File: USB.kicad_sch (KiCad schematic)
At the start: 20 parts, among them J501 USB_A_Stacked, J502 USB_A_Stacked, U501 ASDMB-24.000MHz-C, U502 ASDMB-26.000MHz-C, U503 USB3343, U504 74LVC1G07, U505 USB2514B_Bi

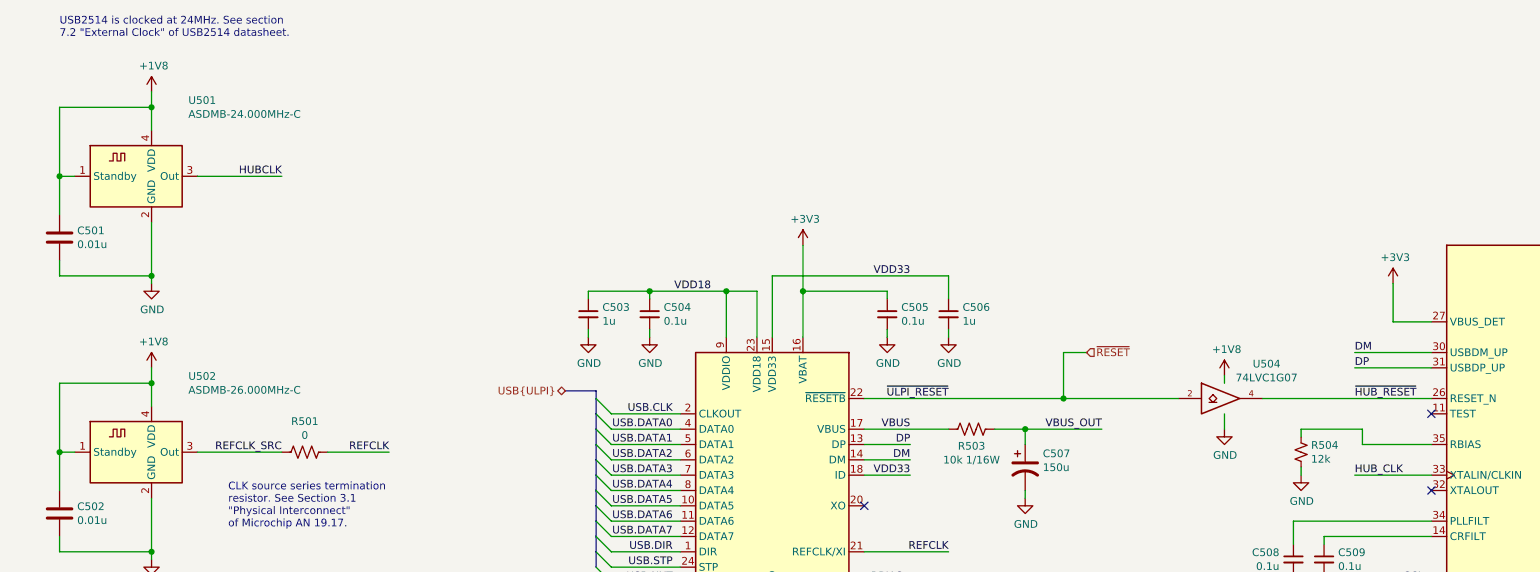
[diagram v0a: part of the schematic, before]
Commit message: Power USB REFCLK from PHY regulator, add pull up resistors to USB reset line
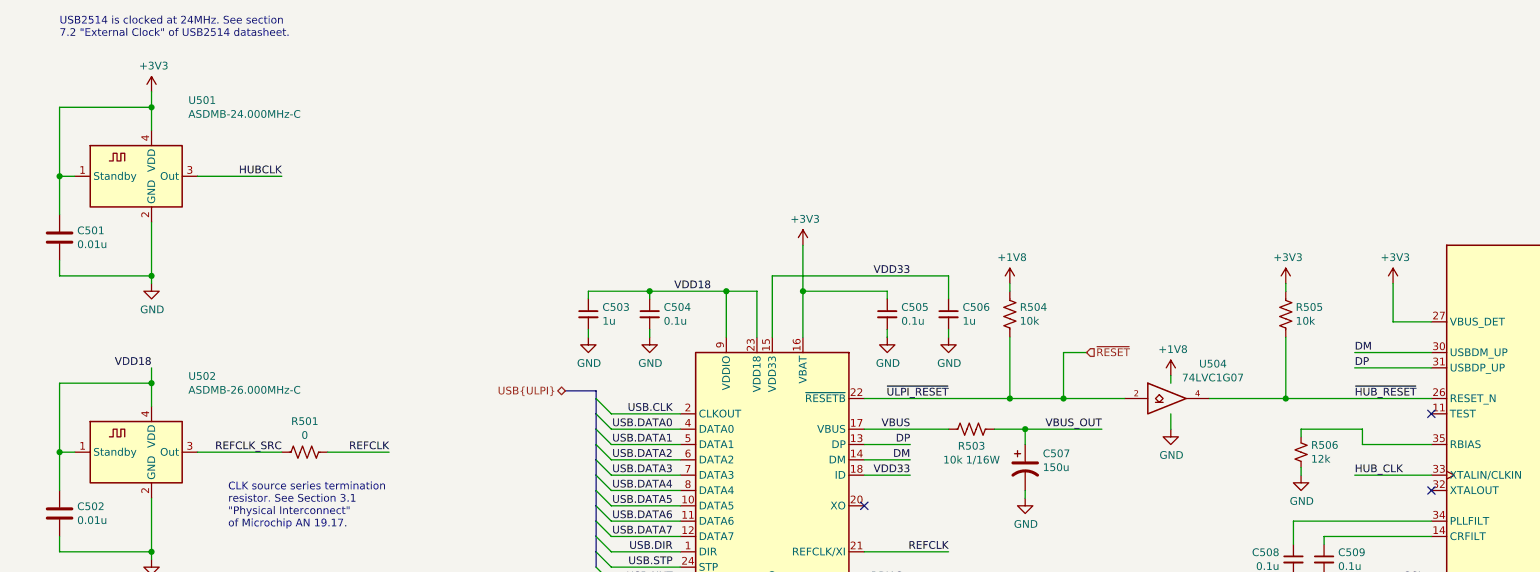
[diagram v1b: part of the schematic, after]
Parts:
- added R504, R505: 10k, Resistor_SMD:R_0402_1005Metric, symbol Device:R_US
- renumbered R504 to R506
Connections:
- net +1V8: now also R504.1; no longer C501.1, C502.1, U501.1 (Standby), U501.4 (VDD), U502.1 (Standby), U502.4 (VDD)
- net +3V3: now also C501.1, U501.1 (Standby), U501.4 (VDD), R505.1
- net VDD18: now also C502.1, U502.1 (Standby), U502.4 (VDD)
- net ~HUB_RESET: now also R505.2
- net ~RESET: now also R504.2
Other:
- moved on the sheet: U504
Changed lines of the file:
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@@
   (junction (at 156.21 99.06) (diameter 1.016) (color 0 0 0 0))
   (junction (at 168.91 99.06) (diameter 1.016) (color 0 0 0 0))
+  (junction (at 203.2 116.84) (diameter 1.016) (color 0 0 0 0))
   (junction (at 205.74 121.92) (diameter 1.016) (color 0 0 0 0))
   (junction (at 212.09 116.84) (diameter 1.016) (color 0 0 0 0))
+  (junction (at 248.92 116.84) (diameter 1.016) (color 0 0 0 0))
   (junction (at 252.73 148.59) (diameter 1.016) (color 0 0 0 0))
-  (no_connect (at 273.05 119.38))
   (no_connect (at 273.05 132.08))
   (no_connect (at 179.07 134.62))
+  (no_connect (at 273.05 119.38))
   (bus_entry (at 134.62 116.84) (size 2.54 2.54)
     (stroke (width 0.1524) (type solid) (color 0 0 0 0))
@@
     (stroke (width 0) (type solid) (color 0 0 0 0))
   )
-  (wire (pts (xy 179.07 116.84) (xy 212.09 116.84))
+  (wire (pts (xy 179.07 116.84) (xy 203.2 116.84))
     (stroke (width 0) (type solid) (color 0 0 0 0))
   )
@@
     (stroke (width 0) (type solid) (color 0 0 0 0))
   )
+  (wire (pts (xy 203.2 97.79) (xy 203.2 99.06))
+    (stroke (width 0) (type solid) (color 0 0 0 0))
+  )
+  (wire (pts (xy 203.2 106.68) (xy 203.2 116.84))
+    (stroke (width 0) (type solid) (color 0 0 0 0))
+  )
+  (wire (pts (xy 203.2 116.84) (xy 212.09 116.84))
+    (stroke (width 0) (type solid) (color 0 0 0 0))
+  )
   (wire (pts (xy 205.74 121.92) (xy 205.74 124.46))
     (stroke (width 0) (type solid) (color 0 0 0 0))
@@
     (stroke (width 0) (type solid) (color 0 0 0 0))
   )
-  (wire (pts (xy 212.09 116.84) (xy 231.14 116.84))
+  (wire (pts (xy 212.09 116.84) (xy 222.25 116.84))
     (stroke (width 0) (type solid) (color 0 0 0 0))
   )
@@
     (stroke (width 0) (type solid) (color 0 0 0 0))
   )
-  (wire (pts (xy 238.76 113.03) (xy 238.76 114.3))
-    (stroke (width 0) (type solid) (color 0 0 0 0))
-  )
-  (wire (pts (xy 238.76 119.38) (xy 238.76 121.92))
-    (stroke (width 0) (type solid) (color 0 0 0 0))
-  )
-  (wire (pts (xy 245.11 116.84) (xy 273.05 116.84))
+  (wire (pts (xy 229.87 113.03) (xy 229.87 114.3))
+    (stroke (width 0) (type solid) (color 0 0 0 0))
+  )
+  (wire (pts (xy 229.87 119.38) (xy 229.87 121.92))
+    (stroke (width 0) (type solid) (color 0 0 0 0))
+  )
+  (wire (pts (xy 236.22 116.84) (xy 248.92 116.84))
+    (stroke (width 0) (type solid) (color 0 0 0 0))
+  )
+  (wire (pts (xy 248.92 97.79) (xy 248.92 99.06))
+    (stroke (width 0) (type solid) (color 0 0 0 0))
+  )
+  (wire (pts (xy 248.92 106.68) (xy 248.92 116.84))
+    (stroke (width 0) (type solid) (color 0 0 0 0))
+  )
+  (wire (pts (xy 248.92 116.84) (xy 273.05 116.84))
     (stroke (width 0) (type solid) (color 0 0 0 0))
   )
@@
     (effects (font (size 1.27 1.27)) (justify right bottom))
   )
+  (label "VDD18" (at 60.96 111.76 180)
+    (effects (font (size 1.27 1.27)) (justify right bottom))
+  )
   (label "HUBCLK" (at 82.55 80.01 180)
     (effects (font (size 1.27 1.27)) (justify right bottom))
@@
     (effects (font (size 1.27 1.27)) (justify right))
   )
-  (symbol (lib_id "power:+1V8") (at 60.96 66.04 0) (unit 1)
+  (symbol (lib_id "power:+3V3") (at 60.96 66.04 0) (unit 1)
     (in_bom yes) (on_board yes)
     (property "Reference" "#PWR?" (id 0) (at 60.96 69.85 0)
       (effects (font (size 1.27 1.27)) hide)
     )
-    (property "Value" "+1V8" (id 1) (at 61.3283 61.7156 0))
+    (property "Value" "+3V3" (id 1) (at 61.3283 61.7156 0))
     (property "Footprint" "" (id 2) (at 60.96 66.04 0)
       (effects (font (size 1.27 1.27)) hide)
     )
     (property "Datasheet" "" (id 3) (at 60.96 66.04 0)
-      (effects (font (size 1.27 1.27)) hide)
-    )
-  )
-  (symbol (lib_id "power:+1V8") (at 60.96 111.76 0) (unit 1)
-    (in_bom yes) (on_board yes)
-    (property "Reference" "#PWR?" (id 0) (at 60.96 115.57 0)
-      (effects (font (size 1.27 1.27)) hide)
-    )
-    (property "Value" "+1V8" (id 1) (at 61.3283 107.4356 0))
-    (property "Footprint" "" (id 2) (at 60.96 111.76 0)
-      (effects (font (size 1.27 1.27)) hide)
-    )
-    (property "Datasheet" "" (id 3) (at 60.96 111.76 0)
       (effects (font (size 1.27 1.27)) hide)
     )
@@
     )
   )
-  (symbol (lib_id "power:+1V8") (at 238.76 113.03 0) (unit 1)
-    (in_bom yes) (on_board yes)
-    (property "Reference" "#PWR?" (id 0) (at 238.76 116.84 0)
-      (effects (font (size 1.27 1.27)) hide)
-    )
-    (property "Value" "+1V8" (id 1) (at 239.1283 108.7056 0))
-    (property "Footprint" "" (id 2) (at 238.76 113.03 0)
-      (effects (font (size 1.27 1.27)) hide)
-    )
-    (property "Datasheet" "" (id 3) (at 238.76 113.03 0)
+  (symbol (lib_id "power:+1V8") (at 203.2 97.79 0) (unit 1)
+    (in_bom yes) (on_board yes)
+    (property "Reference" "#PWR?" (id 0) (at 203.2 101.6 0)
+      (effects (font (size 1.27 1.27)) hide)
+    )
+    (property "Value" "+1V8" (id 1) (at 203.5683 93.4656 0))
+    (property "Footprint" "" (id 2) (at 203.2 97.79 0)
+      (effects (font (size 1.27 1.27)) hide)
+    )
+    (property "Datasheet" "" (id 3) (at 203.2 97.79 0)
+      (effects (font (size 1.27 1.27)) hide)
+    )
+  )
+  (symbol (lib_id "power:+1V8") (at 229.87 113.03 0) (unit 1)
+    (in_bom yes) (on_board yes)
+    (property "Reference" "#PWR?" (id 0) (at 229.87 116.84 0)
+      (effects (font (size 1.27 1.27)) hide)
+    )
+    (property "Value" "+1V8" (id 1) (at 230.2383 108.7056 0))
+    (property "Footprint" "" (id 2) (at 229.87 113.03 0)
+      (effects (font (size 1.27 1.27)) hide)
+    )
+    (property "Datasheet" "" (id 3) (at 229.87 113.03 0)
+      (effects (font (size 1.27 1.27)) hide)
+    )
+  )
+  (symbol (lib_id "power:+3V3") (at 248.92 97.79 0) (unit 1)
+    (in_bom yes) (on_board yes)
+    (property "Reference" "#PWR?" (id 0) (at 248.92 101.6 0)
+      (effects (font (size 1.27 1.27)) hide)
+    )
+    (property "Value" "+3V3" (id 1) (at 249.2883 93.4656 0))
+    (property "Footprint" "" (id 2) (at 248.92 97.79 0)
+      (effects (font (size 1.27 1.27)) hide)
+    )
+    (property "Datasheet" "" (id 3) (at 248.92 97.79 0)
       (effects (font (size 1.27 1.27)) hide)
     )
@@
     )
   )
-  (symbol (lib_id "power:GND") (at 238.76 121.92 0) (unit 1)
-    (in_bom yes) (on_board yes)
-    (property "Reference" "#PWR?" (id 0) (at 238.76 128.27 0)
-      (effects (font (size 1.27 1.27)) hide)
-    )
-    (property "Value" "GND" (id 1) (at 238.8743 126.2444 0))
-    (property "Footprint" "" (id 2) (at 238.76 121.92 0)
-      (effects (font (size 1.27 1.27)) hide)
-    )
-    (property "Datasheet" "" (id 3) (at 238.76 121.92 0)
+  (symbol (lib_id "power:GND") (at 229.87 121.92 0) (unit 1)
+    (in_bom yes) (on_board yes)
+    (property "Reference" "#PWR?" (id 0) (at 229.87 128.27 0)
+      (effects (font (size 1.27 1.27)) hide)
+    )
+    (property "Value" "GND" (id 1) (at 229.9843 126.2444 0))
+    (property "Footprint" "" (id 2) (at 229.87 121.92 0)
+      (effects (font (size 1.27 1.27)) hide)
+    )
+    (property "Datasheet" "" (id 3) (at 229.87 121.92 0)
       (effects (font (size 1.27 1.27)) hide)
     )
@@
   (symbol (lib_id "Device:R_Small_US") (at 251.46 125.73 0) (unit 1)
     (in_bom yes) (on_board yes)
-    (property "Reference" "R504" (id 0) (at 253.1111 124.5806 0)
+    (property "Reference" "R506" (id 0) (at 253.1111 124.5806 0)
       (effects (font (size 1.27 1.27)) (justify left))
     )
@@
     )
   )
+  (symbol (lib_id "Device:R_US") (at 203.2 102.87 0) (unit 1)
+    (in_bom yes) (on_board yes)
+    (property "Reference" "R504" (id 0) (at 204.8511 101.7206 0)
+      (effects (font (size 1.27 1.27)) (justify left))
+    )
+    (property "Value" "10k" (id 1) (at 204.851 104.013 0)
+      (effects (font (size 1.27 1.27)) (justify left))
+    )
+    (property "Footprint" "Resistor_SMD:R_0402_1005Metric" (id 2) (at 204.216 103.124 90)
+      (effects (font (size 1.27 1.27)) hide)
+    )
+    (property "Datasheet" "~" (id 3) (at 203.2 102.87 0)
+      (effects (font (size 1.27 1.27)) hide)
+    )
+  )
+  (symbol (lib_id "Device:R_US") (at 248.92 102.87 0) (unit 1)
+    (in_bom yes) (on_board yes)
+    (property "Reference" "R505" (id 0) (at 250.5711 101.7206 0)
+      (effects (font (size 1.27 1.27)) (justify left))
+    )
+    (property "Value" "10k" (id 1) (at 250.571 104.013 0)
+      (effects (font (size 1.27 1.27)) (justify left))
+    )
+    (property "Footprint" "Resistor_SMD:R_0402_1005Metric" (id 2) (at 249.936 103.124 90)
+      (effects (font (size 1.27 1.27)) hide)
+    )
+    (property "Datasheet" "~" (id 3) (at 248.92 102.87 0)
+      (effects (font (size 1.27 1.27)) hide)
+    )
+  )
   (symbol (lib_id "Device:C_Small") (at 133.35 102.87 0) (unit 1)
     (in_bom yes) (on_board yes)
@@
     )
   )
-  (symbol (lib_id "74xGxx:74LVC1G07") (at 238.76 116.84 0) (unit 1)
-    (in_bom yes) (on_board yes)
-    (property "Reference" "U504" (id 0) (at 245.745 111.1058 0))
-    (property "Value" "74LVC1G07" (id 1) (at 245.745 113.4045 0))
-    (property "Footprint" "Package_TO_SOT_SMD:SOT-553" (id 2) (at 238.76 116.84 0)
-      (effects (font (size 1.27 1.27)) hide)
-    )
-    (property "Datasheet" "http://www.ti.com/lit/sg/scyt129e/scyt129e.pdf" (id 3) (at 238.76 116.84 0)
-      (effects (font (size 1.27 1.27)) hide)
-    )
+  (symbol (lib_id "74xGxx:74LVC1G07") (at 229.87 116.84 0) (unit 1)
+    (in_bom yes) (on_board yes)
+    (property "Reference" "U504" (id 0) (at 236.855 111.1058 0))
+    (property "Value" "74LVC1G07" (id 1) (at 236.855 113.4045 0))
+    (property "Footprint" "Package_TO_SOT_SMD:SOT-553" (id 2) (at 229.87 116.84 0)
+      (effects (font (size 1.27 1.27)) hide)
+    )
+    (property "Datasheet" "http://www.ti.com/lit/sg/scyt129e/scyt129e.pdf" (id 3) (at 229.87 116.84 0)
+      (effects (font (size 1.27 1.27)) hide)
+    )

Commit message: WIP: layout USB host interface
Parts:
- added C508, C509, C518: 4.7u, Capacitor_SMD:C_0402_1005Metric, symbol Device:C_Small
- added C511, C513, C514, C515, C516, C517: 0.01u, Capacitor_SMD:C_0402_1005Metric, symbol Device:C_Small
- added FB501: 120 ohms, Inductor_SMD:L_0603_1608Metric, symbol Device:FerriteBead_Small
- C510: renamed from C508; value 0.1u -> 0.01u
- C512: renamed from C509; value 0.1u -> 0.01u
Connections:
- net VDD18 is gone; now on net +1V8: C502.1, C503.1, C504.1, U502.1 (Standby), U502.4 (VDD), U503.23 (VDD18), U503.9 (VDDIO)
- net +3V3: now also U505.15 (VDD33), U505.23 (VDD33), C508.1, C516.1, C517.1, C518.1, FB501.1
- net D2N: now also J501.7 (D2+); no longer J501.6 (D2-)
- net D2P: now also J501.6 (D2-); no longer J501.7 (D2+)
- net D3N: now also J502.7 (D2+); no longer J502.2 (D1-)
- net D3P: now also J502.6 (D2-); no longer J502.3 (D1+)
- net D4N: now also J502.2 (D1-); no longer J502.6 (D2-)
- net D4P: now also J502.3 (D1+); no longer J502.7 (D2+)
- net GND: now also J501.4 (GND1), J501.8 (GND2), J502.4 (GND1), J502.8 (GND2), C508.2, C509.2, C511.2, C513.2, C514.2, C515.2, C516.2, C517.2, C518.2
- net PLLFILT: now reaches C510.1, U505.34 (PLLFILT)
- net VDDA33: now reaches U505.10 (VDDA33)
- net VDDA33: now also U505.29 (VDDA33), U505.36 (VDDA33), U505.5 (VDDA33), C509.1, C511.1, C513.1, C514.1, C515.1, FB501.2
- net CRFILT: now reaches C512.1, U505.14 (CRFILT)
- net RBIAS_HUB: now reaches R506.1, U505.35 (RBIAS)
- net DM renamed D-
- net DP renamed D+
- net RBIAS renamed RBIAS_PHY
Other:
- note added: "Layout note: Differential pairs 2 and 3 have their polarity swapped to make layout easier."
- note added: "Layout note: place capacitors as close to CRFILT and PLFILT as possible without using vias. See sections CRFILT and PLFILT of USB2514B Schematic Checklist."
- note added: "TODO: VBUS_OUT should be connected to something"
- moved on the sheet: C510, C512, J501, J502, R502, R505, R506, U505
